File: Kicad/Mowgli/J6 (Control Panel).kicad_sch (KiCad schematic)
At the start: 73 parts, among them J6 Control Panel, Q2 NMOS_G15, Q4 NMOS_G15, Q5 NMOS_G15, Q6 NMOS_G15, U2 STM32F030R8T6, U3 AMS1117-3.3

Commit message: Add Rain and Hall possibilities
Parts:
- added FB2: Ferrite_Bead, symbol Device:Ferrite_Bead
- added R1: 4k7, symbol Device:R
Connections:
- net +3.3V: now also R1.2
- net J6_Pin_11_RainSensor: now also FB2.2; no longer JP1.2 (Pin_2)
- net at C8.1, FB1.2: now also JP1.2 (Pin_2); no longer JP1.1 (Pin_1)
- net at U2.60 (BOOT0): now also R1.1
- new net: FB2.1, JP1.1 (Pin_1)
- no-connect marks 0 -> 5
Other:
- note added: "???"
- note added: "Optional Bridge R57 (or move R52) to get Stop Hall (white) to GPIO PC5"
- note added: "Optional Solder Cable to R79/PB1 (ADC_IN9) to get Rain Signal"
- note added: "Optional Solder Cable to U5 (Pin 2) to get Stop Hall (yw) to GPIO PB6"
- note added: "Optional: Solder Cable to U5/Pin-2 to get Signal to PB6"
- note added: "Optional: Solder Cable to U5/Pin-3 to get Signal to PB7"
- note added: "U5-Pin2 (res)"
- note removed: "Rain Sensor"
- note removed: "U5-Pin2"

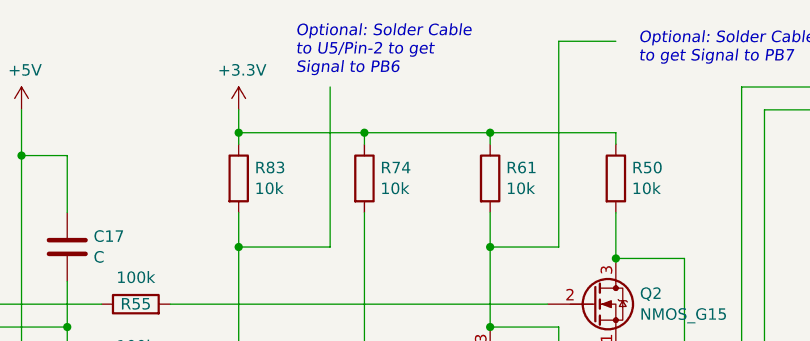
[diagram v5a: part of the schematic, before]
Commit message: Fix MOD instructions
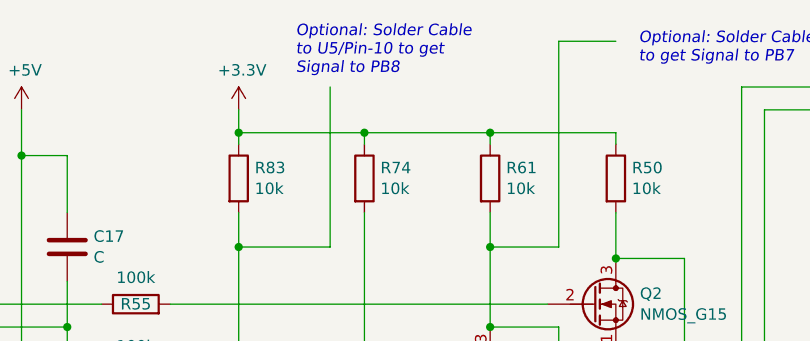
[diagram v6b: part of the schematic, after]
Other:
- note added: "Optional: Solder Cable to U5/Pin-10 to get Signal to PB8"
- note removed: "Optional: Solder Cable to U5/Pin-2 to get Signal to PB6"
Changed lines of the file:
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@@
     (effects (font (size 1.27 1.27)) (justify left bottom))
   )
-  (text "Optional: Solder Cable\nto U5/Pin-2 to get\nSignal to PB6"
+  (text "Optional: Solder Cable\nto U5/Pin-10 to get\nSignal to PB8"
     (at 119.38 20.32 0)
     (effects (font (size 1.27 1.27) italic) (justify left bottom))
